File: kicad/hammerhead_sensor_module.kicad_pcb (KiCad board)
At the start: 6 copper layers, 87.5 x 58.8 mm, 160 parts, among them IC1 RT6254BHGJ6F, IC3 RT6254BHGJ6F, IC4 MAX98357AETE+T, IC6 TXB0108RGYR, J1 COMMS CONN, J10 12402012E212A, J11 10164227-1001A1RLF, J12 10164227-1001A1RLF, J2 APCI0105-P001A, J3 SMN-303, J4 Conn_01x22_Female, J5 Conn_01x22_Female, J6 Conn_01x03, J7 SM04B-SRSS-TBLFSN, J8 SM04B-SRSS-TBLFSN, J9 B6B-XH-A, SW1 218-2LPSTRF, U1 TPD4E05U06DQAR, U10 TPD4E05U06DQAR, U11 TPD4E05U06DQAR, U12 467651001, U13 RT9742SNGV, U14 TPD4E05U06DQAR, U15 TPD4E05U06DQAR, U16 TPD4E05U06DQAR, U17 TPD4E05U06DQAR, U18 TPD4E05U06DQAR, U19 TPD4E05U06DQAR, U2 MMBT3904TT1G, U3 TLV75733PDBVR, U4 TPD4E05U06DQAR, U5 TPD4E05U06DQAR, U6 TPD4E05U06DQAR, U7 TPD4E05U06DQAR, U8 TPD4E05U06DQAR, U9 TPD4E05U06DQAR

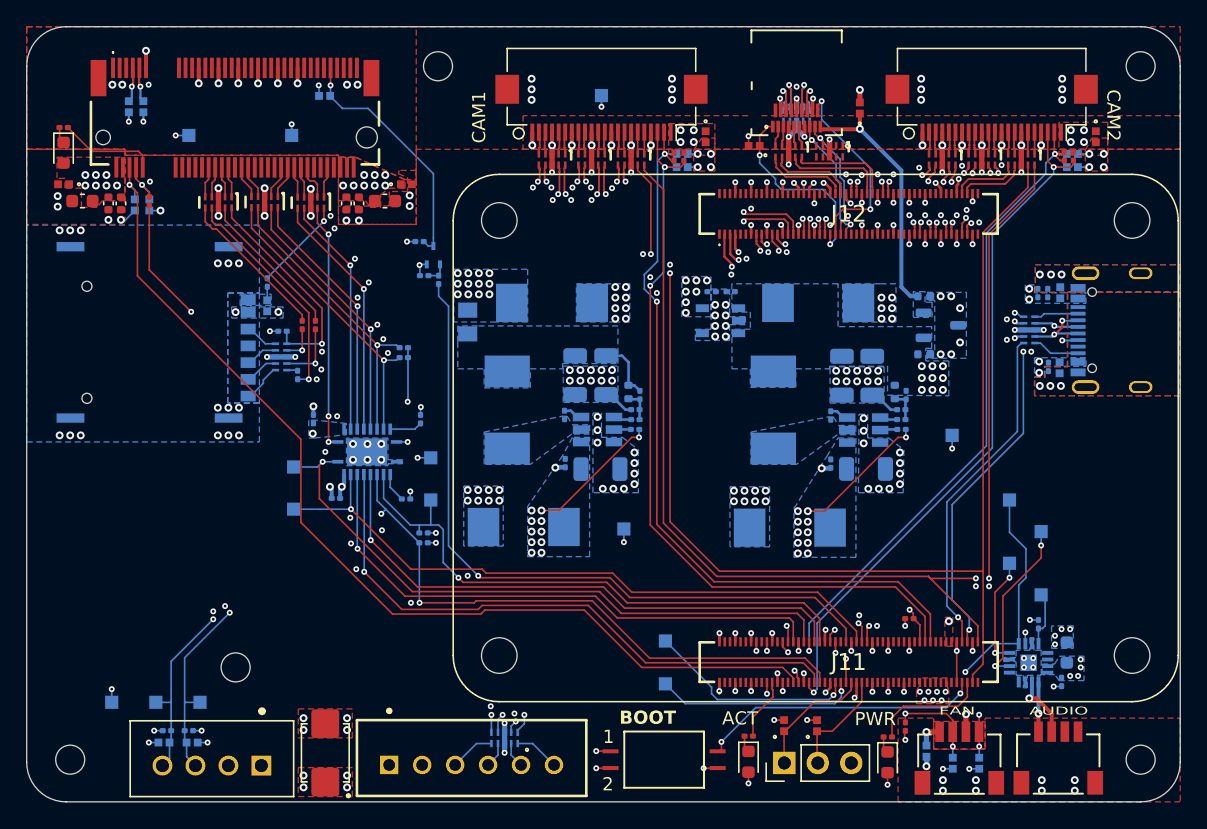
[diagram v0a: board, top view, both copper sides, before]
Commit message: add can controller and transceiver, replace jst connectors with molex micro fit connectors
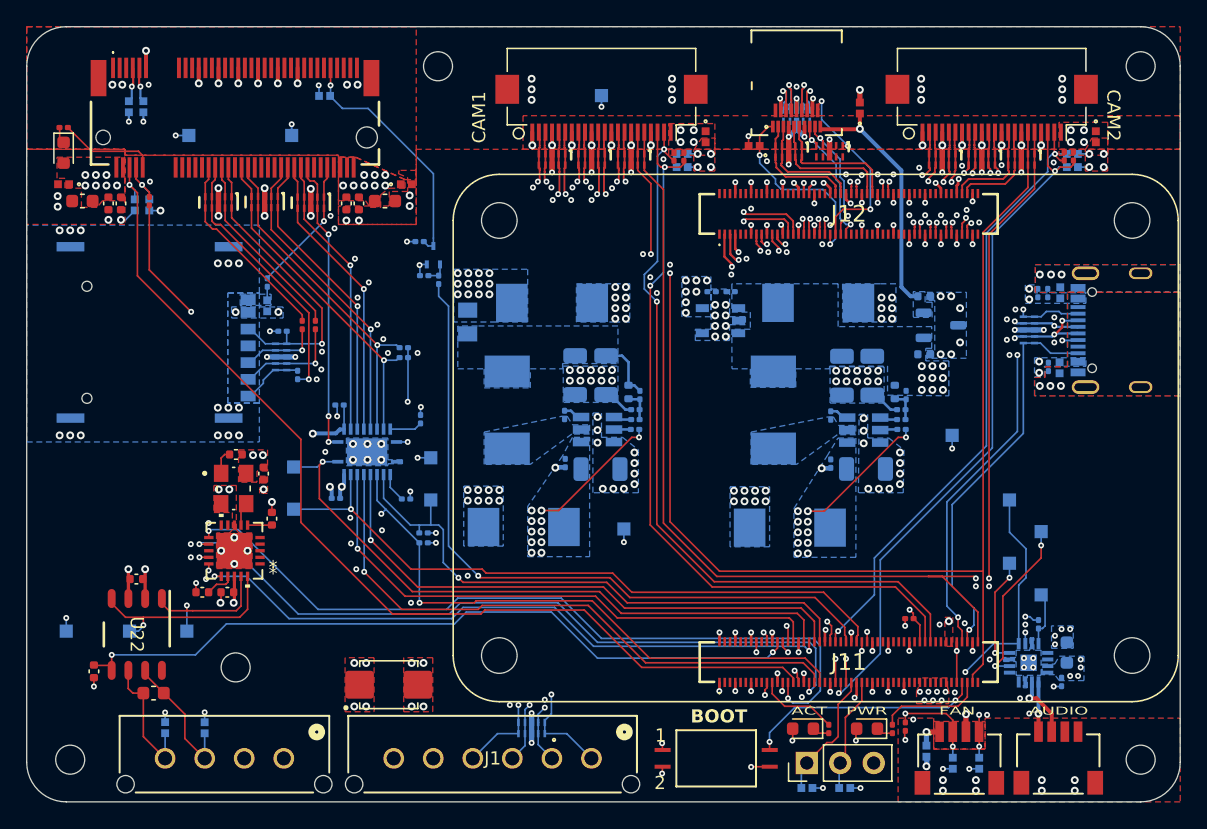
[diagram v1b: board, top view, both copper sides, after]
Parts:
- removed J9: B6B-XH-A, B6B-XH-A:B6BXHA
- removed R1, R2: 2.2k 1%, Resistor_SMD:R_0201_0603Metric
- removed TP17, TP18: TestPoint, TestPoint:TestPoint_Pad_1.0x1.0mm
- added C11: 0.01uF, Capacitor_SMD:C_0402_1005Metric, F.Cu at (75.6, 61.6)
- added C13: 0.1uF, Capacitor_SMD:C_0402_1005Metric, F.Cu at (72.9, 70.7)
- added C33: 0.1uF, Capacitor_SMD:C_0402_1005Metric, F.Cu at (66.0, 69.7)
- added J13: 436500427, 436500427:CONN_SD-43650-010_04_MOL, F.Cu at (77.1, 83.2)
- added R34: 10k, Capacitor_SMD:C_0402_1005Metric, F.Cu at (73.5, 60.2)
- added R35: 10k, Capacitor_SMD:C_0402_1005Metric, F.Cu at (71.0, 70.7)
- added R36: 10k, Capacitor_SMD:C_0402_1005Metric, F.Cu at (62.8, 76.7)
- added R37: 100k, Capacitor_SMD:C_0402_1005Metric, F.Cu at (76.2, 65.1)
- added R38: 120, Capacitor_SMD:C_0603_1608Metric, F.Cu at (67.3, 78.3)
- added U20: MCP2515T-I/ML, MCP2515T_I_ML:QFN20_4x4MC_MCH, F.Cu at (73.4, 67.5)
- added U22: TCAN337DR, TCAN337DR:D0008A_N, F.Cu at (66.0, 73.8)
- added Y1: ASTX-H11-16.000MHZ-I25-T, ASTX_H11_16_000MHZ_I25_T:XTAL_ASTX-H11-16.000MHZ-I25-T, F.Cu at (73.3, 62.8)
- C27: value 100pF -> 0.1uF
- D21, D22: moved to B.Cu
- J1: value COMMS CONN -> 436500616; footprint B4B-XH-A:JST_B4B-XH-A -> 436500616:CONN_SD-43650-006_06_MOL
- moved J1 28.8 mm to (100.5, 83.2)
- moved TP7 7.60 mm to (65.5, 73.6)
- moved D11 7.07 mm to (85.1, 77.7), turned to 0 degrees
- moved TP14 6.41 mm to (60.6, 73.6)
- moved R21 6.10 mm to (118.5, 81.0), turned to 90 degrees
- moved TP8 5.89 mm to (69.8, 73.6)
- moved D22 5.18 mm to (119.7, 85.5), turned to 0 degrees
- moved D21 5.04 mm to (116.8, 85.5), turned to 0 degrees
- moved D10 4.84 mm to (116.5, 81.0), turned to 180 degrees
- moved SW1 3.95 mm to (110.0, 83.2)
- moved D12 2.99 mm to (121.4, 81.0), turned to 180 degrees
- moved C38 2.25 mm to (81.4, 56.5), turned to 180 degrees
- moved U4 2.18 mm to (96.0, 81.0)
- moved J6 1.70 mm to (116.8, 83.6)
- moved D4 1.47 mm to (71.2, 80.9), turned to 90 degrees
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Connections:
- D17 pad 1: /ID_SC -> /I2C_SCL_CAM2
- D18 pad 1: /IC_SD -> /I2C_SDA_CAM2
- D4 pad 1: /PLATFORM_I2C_SDA -> /PLATFORM_CANH
- D6 pad 1: /PLATFORM_I2C_SCL -> /PLATFORM_CANL
- J1 pad 1: 14.8V -> /IR_LED_DIM
- J1 pad 2: GND -> /W_LED_DIM
- J1 pad 3: /PLATFORM_I2C_SDA -> /LASER2
- J1 pad 4: /PLATFORM_I2C_SCL -> /LASER1
- J10 pad A5: Net-(J10-CC1_A) -> /CC1
- J10 pad A6: Net-(J10-D+_A) -> /USB2_P
- J10 pad A7: Net-(J10-D-_A) -> /USB2_N
- J10 pad B5: Net-(J10-CC1_B) -> /CC2
- J10 pad B6: Net-(J10-D+_A) -> /USB2_P
- J10 pad B7: Net-(J10-D-_A) -> /USB2_N
- J11 pad 24: unconnected-(J11-GPIO26-Pad24) -> /CM5_GPIO/CAN_FAULT
- J11 pad 27: unconnected-(J11-GPIO20-Pad27) -> /CM5_GPIO/CAN_INT
- J11 pad 35: /ID_SC -> /CM5_GPIO/CAN_MISO
- J11 pad 36: /IC_SD -> /CM5_GPIO/CAN_CS
- J11 pad 45: /CM5_GPIO/TEST_GPIO_1 -> /LASER2
- J11 pad 46: /LASER2 -> /I2C_SDA_CAM2
- J11 pad 47: /CM5_GPIO/TEST_GPIO_2 -> /I2C_SCL_CAM2
- J11 pad 56: /PLATFORM_I2C_SCL -> /CM5_GPIO/CAN_SCK
- J11 pad 58: /PLATFORM_I2C_SDA -> /CM5_GPIO/CAN_MOSI
- J2 pad 30: Net-(J2-USIM_RST) -> /SIM7600G-H-M2B/USIM_RST
- J2 pad 32: Net-(J2-USIM_CLK) -> /SIM7600G-H-M2B/USIM_CLK
- J2 pad 34: Net-(J2-USIM_DATA) -> /SIM7600G-H-M2B/USIM_DATA
- J2 pad 36: Net-(J2-USIM_VDD) -> /SIM7600G-H-M2B/USIM_VDD
- J2 pad 40: Net-(J2-I2C_SCL) -> /SIM7600G-H-M2B/I2C_SCL
- J2 pad 42: Net-(J2-I2C_SDA) -> /SIM7600G-H-M2B/I2C_SDA
- J2 pad 52: Net-(J2-UART_DTR) -> /SIM7600G-H-M2B/SIM_UART_DTR
- J2 pad 54: Net-(J2-UART_RTS) -> /SIM7600G-H-M2B/SIM_UART_RTS
- J2 pad 56: Net-(J2-UART_CTS) -> /SIM7600G-H-M2B/SIM_UART_CTS
- J2 pad 58: Net-(J2-UART_RXD) -> /SIM7600G-H-M2B/SIM_UART_RXD
- J2 pad 60: Net-(J2-UART_TXD) -> /SIM7600G-H-M2B/SIM_UART_TXD
- J2 pad 66: Net-(J2-USIM_DET) -> /SIM7600G-H-M2B/USIM_CD
- J3 pad C1: Net-(J3-VCC) -> /SIM7600G-H-M2B/USIM_VDD
- J4 pad 11: /CM5_HighSpeed/mipi_csi2_camera_port1/C_D2_N -> /CM5_HighSpeed/DPHY0_D2_N
- J4 pad 12: /CM5_HighSpeed/mipi_csi2_camera_port1/C_D2_P -> /CM5_HighSpeed/DPHY0_D2_P
- J4 pad 14: /CM5_HighSpeed/mipi_csi2_camera_port1/C_D3_N -> /CM5_HighSpeed/DPHY0_D3_N
- J4 pad 15: /CM5_HighSpeed/mipi_csi2_camera_port1/C_D3_P -> /CM5_HighSpeed/DPHY0_D3_P
- J4 pad 17: Net-(J4-Pin_17) -> /CAM_GPIO0
- J4 pad 18: Net-(J4-Pin_18) -> /CAM_GPIO1
- J4 pad 2: /CM5_HighSpeed/mipi_csi2_camera_port1/C_D0_N -> /CM5_HighSpeed/DPHY0_D0_N
- J4 pad 3: /CM5_HighSpeed/mipi_csi2_camera_port1/C_D0_P -> /CM5_HighSpeed/DPHY0_D0_P
- J4 pad 5: /CM5_HighSpeed/mipi_csi2_camera_port1/C_D1_N -> /CM5_HighSpeed/DPHY0_D1_N
- J4 pad 6: /CM5_HighSpeed/mipi_csi2_camera_port1/C_D1_P -> /CM5_HighSpeed/DPHY0_D1_P
- J4 pad 8: /CM5_HighSpeed/mipi_csi2_camera_port1/C_C_N -> /CM5_HighSpeed/DPHY0_C_N
- J4 pad 9: /CM5_HighSpeed/mipi_csi2_camera_port1/C_C_P -> /CM5_HighSpeed/DPHY0_C_P
- J5 pad 11: /CM5_HighSpeed/mipi_csi2_camera_port2/C_D2_N -> /CM5_HighSpeed/DPHY1_D2_N
- J5 pad 12: /CM5_HighSpeed/mipi_csi2_camera_port2/C_D2_P -> /CM5_HighSpeed/DPHY1_D2_P
- J5 pad 14: /CM5_HighSpeed/mipi_csi2_camera_port2/C_D3_N -> /CM5_HighSpeed/DPHY1_D3_N
- J5 pad 15: /CM5_HighSpeed/mipi_csi2_camera_port2/C_D3_P -> /CM5_HighSpeed/DPHY1_D3_P
- J5 pad 17: Net-(J5-Pin_17) -> /CAM_GPIO0
- J5 pad 18: Net-(J5-Pin_18) -> /CAM_GPIO1
- J5 pad 2: /CM5_HighSpeed/mipi_csi2_camera_port2/C_D0_N -> /CM5_HighSpeed/DPHY1_D0_N
- J5 pad 20: /ID_SC -> /I2C_SCL_CAM2
- J5 pad 21: /IC_SD -> /I2C_SDA_CAM2
- J5 pad 3: /CM5_HighSpeed/mipi_csi2_camera_port2/C_D0_P -> /CM5_HighSpeed/DPHY1_D0_P
- J5 pad 5: /CM5_HighSpeed/mipi_csi2_camera_port2/C_D1_N -> /CM5_HighSpeed/DPHY1_D1_N
- J5 pad 6: /CM5_HighSpeed/mipi_csi2_camera_port2/C_D1_P -> /CM5_HighSpeed/DPHY1_D1_P
- J5 pad 8: /CM5_HighSpeed/mipi_csi2_camera_port2/C_C_N -> /CM5_HighSpeed/DPHY1_C_N
- J5 pad 9: /CM5_HighSpeed/mipi_csi2_camera_port2/C_C_P -> /CM5_HighSpeed/DPHY1_C_P
- R17 pad 1: Net-(R17-Pad1) -> Net-(J3-RST)
- R19 pad 1: Net-(R19-Pad1) -> Net-(J3-I/O)
- R23 pad 2: /IC_SD -> /I2C_SDA_CAM2
- R24 pad 2: /ID_SC -> /I2C_SCL_CAM2
- R32 pad 1: Net-(R32-Pad1) -> Net-(J3-CLK)
- TP7 pad 1: /PLATFORM_I2C_SDA -> /CM5_GPIO/CAN Controller and Transceiver/RXCAN
- TP8 pad 1: /PLATFORM_I2C_SCL -> /CM5_GPIO/CAN Controller and Transceiver/TXCAN
- U10 pad 1: /CM5_HighSpeed/mipi_csi2_camera_port2/C_D2_P -> /CM5_HighSpeed/DPHY1_D2_P
- U10 pad 2: /CM5_HighSpeed/mipi_csi2_camera_port2/C_D2_N -> /CM5_HighSpeed/DPHY1_D2_N
- U10 pad 4: /CM5_HighSpeed/mipi_csi2_camera_port2/C_C_P -> /CM5_HighSpeed/DPHY1_C_P
- U10 pad 5: /CM5_HighSpeed/mipi_csi2_camera_port2/C_C_N -> /CM5_HighSpeed/DPHY1_C_N
- U11 pad 1: Net-(J4-Pin_18) -> /CAM_GPIO1
- U11 pad 2: Net-(J4-Pin_17) -> /CAM_GPIO0
- U11 pad 4: /CM5_HighSpeed/mipi_csi2_camera_port1/C_D3_P -> /CM5_HighSpeed/DPHY0_D3_P
- U11 pad 5: /CM5_HighSpeed/mipi_csi2_camera_port1/C_D3_N -> /CM5_HighSpeed/DPHY0_D3_N
- U12 pad 11: /CM5_HighSpeed/hdmi/TMDS_DATA0- -> /CM5_HighSpeed/HDMI1_D0_N
- U12 pad 3: /CM5_HighSpeed/hdmi/TMDS_DATA2+ -> /CM5_HighSpeed/HDMI1_D2_P
- U12 pad 5: /CM5_HighSpeed/hdmi/TMDS_DATA2- -> /CM5_HighSpeed/HDMI1_D2_N
- U12 pad 9: /CM5_HighSpeed/hdmi/TMDS_DATA0+ -> /CM5_HighSpeed/HDMI1_D0_P
- U14 pad 1: Net-(J5-Pin_18) -> /CAM_GPIO1
- U14 pad 2: Net-(J5-Pin_17) -> /CAM_GPIO0
- U14 pad 4: /CM5_HighSpeed/mipi_csi2_camera_port2/C_D3_P -> /CM5_HighSpeed/DPHY1_D3_P
- U14 pad 5: /CM5_HighSpeed/mipi_csi2_camera_port2/C_D3_N -> /CM5_HighSpeed/DPHY1_D3_N
- U15 pad 1: /CM5_HighSpeed/hdmi/TMDS_DATA0- -> /CM5_HighSpeed/HDMI1_D0_N
- U15 pad 2: /CM5_HighSpeed/hdmi/TMDS_DATA0+ -> /CM5_HighSpeed/HDMI1_D0_P
- U15 pad 4: /CM5_HighSpeed/hdmi/TMDS_DATA2- -> /CM5_HighSpeed/HDMI1_D2_N
- U15 pad 5: /CM5_HighSpeed/hdmi/TMDS_DATA2+ -> /CM5_HighSpeed/HDMI1_D2_P
- U16 pad 1: Net-(J10-CC1_A) -> /CC1
- U16 pad 10: /CC2 -> /CC1
- U16 pad 2: Net-(J10-D+_A) -> /USB2_P
- U16 pad 4: Net-(J10-D-_A) -> /USB2_N
- U16 pad 5: Net-(J10-CC1_B) -> /CC2
- U16 pad 6: /CC1 -> /CC2
- U17 pad 10: Net-(R32-Pad1) -> Net-(J3-CLK)
- U17 pad 5: Net-(J3-VCC) -> /SIM7600G-H-M2B/USIM_VDD
- U17 pad 7: Net-(R17-Pad1) -> Net-(J3-RST)
- U17 pad 9: Net-(R19-Pad1) -> Net-(J3-I/O)
- U18 pad 1: Net-(J2-UART_RTS) -> /SIM7600G-H-M2B/SIM_UART_RTS
- U18 pad 2: Net-(J2-UART_DTR) -> /SIM7600G-H-M2B/SIM_UART_DTR
- U18 pad 4: Net-(J2-I2C_SDA) -> /SIM7600G-H-M2B/I2C_SDA
- U18 pad 5: Net-(J2-I2C_SCL) -> /SIM7600G-H-M2B/I2C_SCL
- U19 pad 1: Net-(J2-USIM_VDD) -> /SIM7600G-H-M2B/USIM_VDD
- U19 pad 2: Net-(J2-USIM_DATA) -> /SIM7600G-H-M2B/USIM_DATA
- U19 pad 4: Net-(J2-USIM_CLK) -> /SIM7600G-H-M2B/USIM_CLK
- U19 pad 5: Net-(J2-USIM_RST) -> /SIM7600G-H-M2B/USIM_RST
- U4 pad 1: Net-(U4-D1+) -> /IR_LED_DIM
- U4 pad 2: Net-(U4-D1-) -> /W_LED_DIM
- U4 pad 4: Net-(U4-D2+) -> /LASER2
- U4 pad 5: Net-(U4-D2-) -> /LASER1
- U6 pad 1: Net-(J2-USIM_DET) -> /SIM7600G-H-M2B/USIM_CD
- U6 pad 2: Net-(J2-UART_TXD) -> /SIM7600G-H-M2B/SIM_UART_TXD
- U6 pad 4: Net-(J2-UART_RXD) -> /SIM7600G-H-M2B/SIM_UART_RXD
- U6 pad 5: Net-(J2-UART_CTS) -> /SIM7600G-H-M2B/SIM_UART_CTS
- U7 pad 1: /CM5_HighSpeed/mipi_csi2_camera_port2/C_D1_P -> /CM5_HighSpeed/DPHY1_D1_P
- U7 pad 2: /CM5_HighSpeed/mipi_csi2_camera_port2/C_D1_N -> /CM5_HighSpeed/DPHY1_D1_N
- U7 pad 4: /CM5_HighSpeed/mipi_csi2_camera_port2/C_D0_P -> /CM5_HighSpeed/DPHY1_D0_P
- U7 pad 5: /CM5_HighSpeed/mipi_csi2_camera_port2/C_D0_N -> /CM5_HighSpeed/DPHY1_D0_N
- U8 pad 1: /CM5_HighSpeed/mipi_csi2_camera_port1/C_D1_P -> /CM5_HighSpeed/DPHY0_D1_P
- U8 pad 2: /CM5_HighSpeed/mipi_csi2_camera_port1/C_D1_N -> /CM5_HighSpeed/DPHY0_D1_N
- U8 pad 4: /CM5_HighSpeed/mipi_csi2_camera_port1/C_D0_P -> /CM5_HighSpeed/DPHY0_D0_P
- U8 pad 5: /CM5_HighSpeed/mipi_csi2_camera_port1/C_D0_N -> /CM5_HighSpeed/DPHY0_D0_N
- U9 pad 1: /CM5_HighSpeed/mipi_csi2_camera_port1/C_D2_P -> /CM5_HighSpeed/DPHY0_D2_P
- U9 pad 2: /CM5_HighSpeed/mipi_csi2_camera_port1/C_D2_N -> /CM5_HighSpeed/DPHY0_D2_N
- U9 pad 4: /CM5_HighSpeed/mipi_csi2_camera_port1/C_C_P -> /CM5_HighSpeed/DPHY0_C_P
- U9 pad 5: /CM5_HighSpeed/mipi_csi2_camera_port1/C_C_N -> /CM5_HighSpeed/DPHY0_C_N
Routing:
- net /PLATFORM_I2C_SDA: track 65.8 -> 0.00 mm, vias 2 -> 0
- net /PLATFORM_I2C_SCL: track 65.3 -> 0.00 mm, vias 2 -> 0
- net /CM5_GPIO/CAN_INT: track 0.00 -> 58.9 mm, vias 0 -> 2
- net /CM5_GPIO/CAN_FAULT: track 0.00 -> 57.0 mm, vias 0 -> 2
- net /CM5_GPIO/CAN_MISO: track 0.00 -> 55.7 mm, vias 0 -> 2
- net /CM5_GPIO/CAN_MOSI: track 0.00 -> 54.5 mm, vias 0 -> 2
- net /ID_SC: track 54.2 -> 0.00 mm, vias 2 -> 0
- net /CM5_GPIO/CAN_SCK: track 0.00 -> 54.1 mm, vias 0 -> 2
- net /I2C_SCL_CAM2: track 0.00 -> 53.6 mm, vias 0 -> 2
- net /IC_SD: track 49.7 -> 0.00 mm, vias 2 -> 0
- net /CM5_GPIO/CAN_CS: track 0.00 -> 49.3 mm, vias 0 -> 2
- net /I2C_SDA_CAM2: track 0.00 -> 47.6 mm, vias 0 -> 2
- net /CM5_GPIO/TEST_GPIO_1: track 16.0 -> 0.00 mm, vias 1 -> 0
- net /CM5_GPIO/CAN Controller and Transceiver/RXCAN: track 0.00 -> 15.8 mm, vias 0 -> 1
- net /CM5_GPIO/TEST_GPIO_2: track 15.3 -> 0.00 mm, vias 1 -> 0
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- removed copper zone on B.Cu, net 1.8V
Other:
- board text removed: "${REFERENCE}"

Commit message: add can controller and transceiver, replace platform power connector with one with more appropriate current rating, add return vias
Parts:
- removed J7: SM04B-SRSS-TBLFSN, SM04B-SRSS-TB:CONN_SM04B_JST
- added GND1: TestPoint, TestPoint:TestPoint_Pad_1.0x1.0mm, B.Cu at (77.8, 78.2)
- added GND2: TestPoint, TestPoint:TestPoint_Pad_1.0x1.0mm, B.Cu at (135.3, 43.4)
- added GND3: TestPoint, TestPoint:TestPoint_Pad_1.0x1.0mm, B.Cu at (88.2, 36.0)
- added GND4: TestPoint, TestPoint:TestPoint_Pad_1.0x1.0mm, B.Cu at (126.3, 66.2)
- added J9: BM04B-SRSS-TB_LF__SN_, BM04B-SRSS-TB_LF__SN_:BM04B-SRSS-TB_LFSN_, F.Cu at (138.9, 82.3)
- added TP17: TestPoint, TestPoint:TestPoint_Pad_1.0x1.0mm, B.Cu at (77.8, 74.2)
- added TP18: TestPoint, TestPoint:TestPoint_Pad_1.0x1.0mm, B.Cu at (80.8, 70.8)
- added TP19: TestPoint, TestPoint:TestPoint_Pad_1.0x1.0mm, B.Cu at (82.2, 74.2)
- added TP20: TestPoint, TestPoint:TestPoint_Pad_1.0x1.0mm, B.Cu at (77.9, 67.5)
- added TP21: TestPoint, TestPoint:TestPoint_Pad_1.0x1.0mm, B.Cu at (129.1, 45.5)
- added TP22: TestPoint, TestPoint:TestPoint_Pad_1.0x1.0mm, B.Cu at (125.2, 45.5)
- added TP23: TestPoint, TestPoint:TestPoint_Pad_1.0x1.0mm, B.Cu at (106.3, 77.3)
- added TP24: TestPoint, TestPoint:TestPoint_Pad_1.0x1.0mm, B.Cu at (101.0, 77.3)
- C27: value 0.1uF -> 100pF
- J8: value SM04B-SRSS-TBLFSN -> BM04B-SRSS-TB_LF__SN_; footprint SM04B-SRSS-TB:CONN_SM04B_JST -> BM04B-SRSS-TB_LF__SN_:BM04B-SRSS-TB_LFSN_
- R34, R35, R36, R37: footprint Capacitor_SMD:C_0402_1005Metric -> Resistor_SMD:R_0402_1005Metric
- R38: footprint Capacitor_SMD:C_0603_1608Metric -> Resistor_SMD:R_0603_1608Metric
- moved C27 12.4 mm to (82.0, 32.9), turned to 0 degrees
- moved J8 3.19 mm to (131.4, 82.3), turned to 180 degrees
- moved D15 1.12 mm to (128.9, 84.2)
- moved D16 0.60 mm to (127.9, 84.2)
- moved D9 0.60 mm to (125.9, 83.3)
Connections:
- J11 pad 41: unconnected-(J11-GPIO25-Pad41) -> /TEST_GPIO_1
- J11 pad 48: unconnected-(J11-GPIO27-Pad48) -> /TEST_GPIO_2
- J8 pad 1: Net-(IC4-OUTP) -> /CM5_GPIO/TACHO
- J8 pad 2: Net-(IC4-OUTN) -> GND
- J8 pad 3: unconnected-(J8-Pad3) -> /CM5_GPIO/PWM
- J8 pad 4: unconnected-(J8-Pad4) -> 5V
- U20 pad 12: /CM5_GPIO/CAN_MISO -> /CM5_GPIO/CAN_SCK
- U20 pad 15: /CM5_GPIO/CAN_SCK -> /CM5_GPIO/CAN_MISO
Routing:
- net /TEST_GPIO_2: track 0.00 -> 22.5 mm, vias 0 -> 3
- net /TEST_GPIO_1: track 0.00 -> 14.4 mm, vias 0 -> 1
- net /CM5_GPIO/CAN_SCK: track 54.1 -> 59.1 mm, vias 2 -> 3
- net GND: track 136.8 -> 141.3 mm, vias 381 -> 389
- net /CM5_GPIO/CAN_MISO: track 55.7 -> 59.4 mm, vias 2 -> 4
- net /CM5_GPIO/CAN_CS: track 49.3 -> 52.4 mm, vias 2 -> 4
- net /USB2_P: track 34.3 -> 36.2 mm, vias 4 -> 5
- net /USB2_N: track 34.1 -> 35.7 mm, vias 4 -> 5
- net /CM5_GPIO/CAN_MOSI: track 54.5 -> 55.9 mm, vias 2 -> 3
- net /PLATFORM_CANL: track 11.0 -> 12.3 mm

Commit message: add board bringup redlines
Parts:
- added R1: 10k, Resistor_SMD:R_0201_0603Metric, B.Cu at (109.6, 52.2)
- C46: moved to B.Cu
- moved D9 4.97 mm to (130.9, 83.3)
- moved C46 2.84 mm to (125.8, 75.2)
- moved D15 1.05 mm to (127.9, 84.2)
- moved D16 1.05 mm to (128.9, 84.2)
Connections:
- C46 pad 1: 3.3V -> /GPIO_VREF
- J11 pad 78: 3.3V -> /GPIO_VREF
- J11 pad 84: unconnected-(J11-+3.3v_(Output)_600mA_Max-Pad84) -> /GPIO_VREF
- J11 pad 86: unconnected-(J11-+3.3v_(Output)_600mA_Max-Pad86) -> /GPIO_VREF
- J11 pad 92: GND -> unconnected-(J11-PWR_BUT-Pad92)
- J8 pad 1: /CM5_GPIO/TACHO -> 5V
- J8 pad 2: GND -> /CM5_GPIO/PWM
- J8 pad 3: /CM5_GPIO/PWM -> GND
- J8 pad 4: 5V -> /CM5_GPIO/TACHO
- U3 pad 3: 5V -> /GPIO_VREF
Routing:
- net /GPIO_VREF: track 0.00 -> 37.6 mm, vias 0 -> 3
- net 3.3V: track 37.1 -> 33.7 mm
- net /CM5_GPIO/TACHO: track 24.4 -> 21.7 mm
- net /CM5_GPIO/PWM: track 19.6 -> 21.1 mm
- net GND: track 141.3 -> 140.0 mm, vias 389 -> 387
- added copper zone on F.Cu, net /GPIO_VREF
